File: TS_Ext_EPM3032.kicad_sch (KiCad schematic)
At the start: 52 parts, among them J1 JTAG, J2 CD_IN, J3 System Ext, J4 AUDIO OUT, J5 AudioJack3_SwitchTR, Q1 BC547, U1 EPM3064ALC44, U2 AMS1117, U3 YM2149, U4 YM2149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

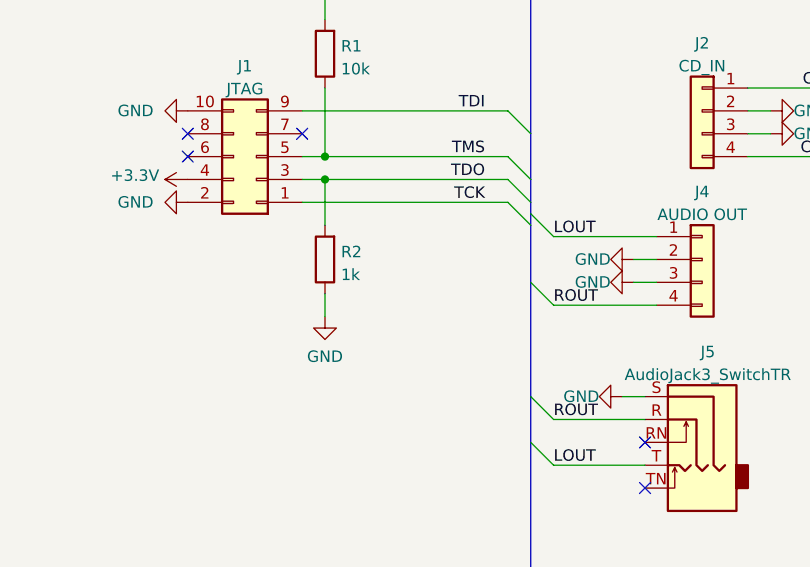
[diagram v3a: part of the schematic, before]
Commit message: Fix pull-up on JTAG connector
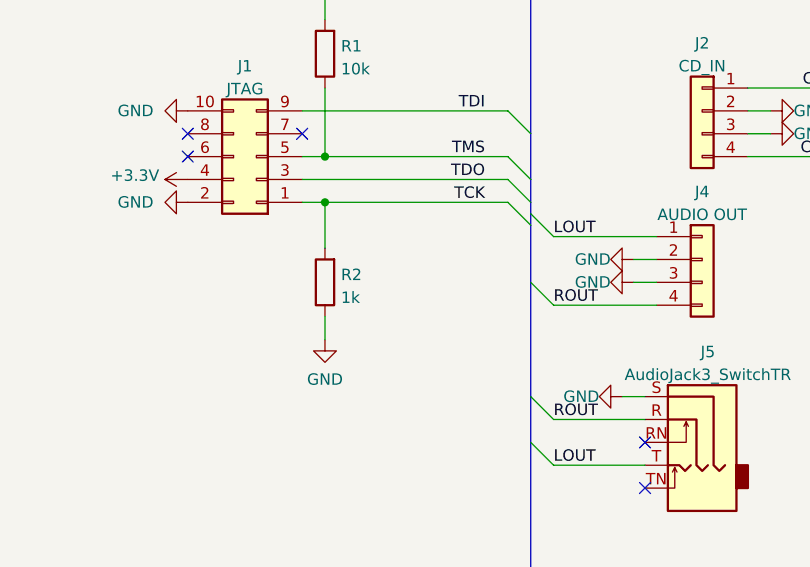
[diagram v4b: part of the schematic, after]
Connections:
- net TCK: now also R2.2
- net TDO: no longer R2.2
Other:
- moved on the sheet: R2
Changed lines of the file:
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@@
   (title_block
     (title "TurboSound Extension Card EPM3032")
-    (date "2022-11-06")
-    (rev "1.2")
+    (date "2023-01-24")
+    (rev "1.3")
     (company "ponchick")
     (comment 1 "Original schematic and firmware by MikhaelK")
@@
   (junction (at 297.18 102.87) (diameter 0) (color 0 0 0 0)
   )
+  (junction (at 78.74 144.78) (diameter 0) (color 0 0 0 0)
+  )
   (junction (at 139.7 266.7) (diameter 0) (color 0 0 0 0)
   )
@@
   (junction (at 129.54 45.72) (diameter 0) (color 0 0 0 0)
   )
-  (junction (at 78.74 142.24) (diameter 0) (color 0 0 0 0)
-  )
   (junction (at 271.78 60.96) (diameter 0) (color 0 0 0 0)
   )
@@
     (stroke (width 0) (type default) (color 0 0 0 0))
   )
-  (wire (pts (xy 78.74 157.48) (xy 78.74 154.94))
+  (wire (pts (xy 78.74 160.02) (xy 78.74 157.48))
     (stroke (width 0) (type default) (color 0 0 0 0))
   )
@@
     (stroke (width 0) (type default) (color 0 0 0 0))
   )
+  (wire (pts (xy 78.74 144.78) (xy 76.2 144.78))
+    (stroke (width 0) (type default) (color 0 0 0 0))
+  )
   (wire (pts (xy 142.24 147.32) (xy 152.4 147.32))
     (stroke (width 0) (type default) (color 0 0 0 0))
@@
     (stroke (width 0) (type default) (color 0 0 0 0))
   )
-  (wire (pts (xy 78.74 142.24) (xy 78.74 147.32))
+  (wire (pts (xy 78.74 144.78) (xy 78.74 149.86))
     (stroke (width 0) (type default) (color 0 0 0 0))
   )
@@
     (stroke (width 0) (type default) (color 0 0 0 0))
   )
-  (wire (pts (xy 99.06 144.78) (xy 76.2 144.78))
+  (wire (pts (xy 99.06 144.78) (xy 78.74 144.78))
     (stroke (width 0) (type default) (color 0 0 0 0))
   )
@@
     (stroke (width 0) (type default) (color 0 0 0 0))
   )
-  (wire (pts (xy 78.74 142.24) (xy 76.2 142.24))
-    (stroke (width 0) (type default) (color 0 0 0 0))
-  )
   (wire (pts (xy 142.24 139.7) (xy 152.4 139.7))
     (stroke (width 0) (type default) (color 0 0 0 0))
@@
     (stroke (width 0) (type default) (color 0 0 0 0))
   )
-  (wire (pts (xy 99.06 142.24) (xy 78.74 142.24))
+  (wire (pts (xy 76.2 142.24) (xy 99.06 142.24))
     (stroke (width 0) (type default) (color 0 0 0 0))
   )
@@
     (pin "2")
   )
-  (symbol (lib_id "power:GND") (at 78.74 157.48 0) (unit 1)
+  (symbol (lib_id "power:GND") (at 78.74 160.02 0) (unit 1)
     (in_bom yes) (on_board yes) (fields_autoplaced)
-    (property "Reference" "#PWR08" (id 0) (at 78.74 163.83 0)
+    (property "Reference" "#PWR08" (id 0) (at 78.74 166.37 0)
       (effects (font (size 1.27 1.27)) hide)
     )
-    (property "Value" "GND" (id 1) (at 78.74 161.9234 0))
-    (property "Footprint" "" (id 2) (at 78.74 157.48 0)
+    (property "Value" "GND" (id 1) (at 78.74 164.4634 0))
+    (property "Footprint" "" (id 2) (at 78.74 160.02 0)
       (effects (font (size 1.27 1.27)) hide)
     )
-    (property "Datasheet" "" (id 3) (at 78.74 157.48 0)
+    (property "Datasheet" "" (id 3) (at 78.74 160.02 0)
       (effects (font (size 1.27 1.27)) hide)
     )
@@
     (pin "8")
   )
-  (symbol (lib_id "Device:R") (at 78.74 151.13 180) (unit 1)
+  (symbol (lib_id "Device:R") (at 78.74 153.67 180) (unit 1)
     (in_bom yes) (on_board yes) (fields_autoplaced)
-    (property "Reference" "R2" (id 0) (at 80.518 150.2953 0)
+    (property "Reference" "R2" (id 0) (at 80.518 152.8353 0)
       (effects (font (size 1.27 1.27)) (justify right))
     )
-    (property "Value" "1k" (id 1) (at 80.518 152.8322 0)
+    (property "Value" "1k" (id 1) (at 80.518 155.3722 0)
       (effects (font (size 1.27 1.27)) (justify right))
     )
-    (property "Footprint" "Resistor_THT:R_Axial_DIN0204_L3.6mm_D1.6mm_P7.62mm_Horizontal" (id 2) (at 80.518 151.13 90)
+    (property "Footprint" "Resistor_THT:R_Axial_DIN0204_L3.6mm_D1.6mm_P7.62mm_Horizontal" (id 2) (at 80.518 153.67 90)
       (effects (font (size 1.27 1.27)) hide)
     )
-    (property "Datasheet" "~" (id 3) (at 78.74 151.13 0)
+    (property "Datasheet" "~" (id 3) (at 78.74 153.67 0)
       (effects (font (size 1.27 1.27)) hide)
     )

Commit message: Migrated to KiCad 8, CPLD value fix
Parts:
- J3: now left out of the parts list
- J5: value AudioJack3_SwitchTR -> SJ1-3525N; symbol Connector:AudioJack3_SwitchTR -> Connector_Audio:AudioJack3_SwitchTR
- U1: value EPM3064ALC44 -> EPM3032ALC44
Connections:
- net ~{RDR}: no longer names the net of J3.b15 (Pin_b15)
- no-connect marks 83 -> 84
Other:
- moved on the sheet: J4, J5

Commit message: Change C13/C14 to electrolytic
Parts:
- C13, C14: footprint Capacitor_THT:C_Rect_L7.0mm_W2.0mm_P5.00mm -> Capacitor_THT:CP_Radial_D5.0mm_P2.50mm; symbol Device:C -> Device:C_Polarized
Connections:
- net ROUT: now also C14.2; no longer C14.1
- net at R24.2, U5.7: now also C14.1; no longer C14.2
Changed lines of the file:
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@@
 		(title "TurboSound Extension Card EPM3032")
 		(date "2024-04-10")
-		(rev "1.4")
+		(rev "1.5")
 		(company "ponchick")
 		(comment 1 "Original schematic and firmware by MikhaelK")
@@
 	)
 	(symbol
-		(lib_id "Device:C")
-		(at 325.12 100.33 270)
+		(lib_id "Device:C_Polarized")
+		(at 325.12 100.33 90)
 		(unit 1)
 		(exclude_from_sim no)
@@
 		(fields_autoplaced yes)
 		(property "Reference" "C14"
-			(at 325.12 94.4712 90)
+			(at 324.231 92.71 90)
 			(effects
 				(font
@@
 		)
 		(property "Value" "10u"
-			(at 325.12 97.0081 90)
+			(at 324.231 95.25 90)
 			(effects
 				(font
@@
 			)
 		)
-		(property "Footprint" "Capacitor_THT:C_Rect_L7.0mm_W2.0mm_P5.00mm"
-			(at 321.31 101.2952 0)
+		(property "Footprint" "Capacitor_THT:CP_Radial_D5.0mm_P2.50mm"
+			(at 328.93 99.3648 0)
 			(effects
 				(font
@@
 			)
 		)
-		(property "Datasheet" ""
+		(property "Datasheet" "~"
 			(at 325.12 100.33 0)
 			(effects
@@
 			)
 		)
-		(property "Description" ""
+		(property "Description" "Polarized capacitor"
 			(at 325.12 100.33 0)
 			(effects
@@
 	)
 	(symbol
-		(lib_id "Device:C")
+		(lib_id "Device:C_Polarized")
 		(at 325.12 53.34 90)
 		(unit 1)
@@
 		(fields_autoplaced yes)
 		(property "Reference" "C13"
-			(at 325.12 47.4812 90)
+			(at 324.231 45.72 90)
 			(effects
 				(font
@@
 		)
 		(property "Value" "10u"
-			(at 325.12 50.0181 90)
+			(at 324.231 48.26 90)
 			(effects
 				(font
@@
 			)
 		)
-		(property "Footprint" "Capacitor_THT:C_Rect_L7.0mm_W2.0mm_P5.00mm"
+		(property "Footprint" "Capacitor_THT:CP_Radial_D5.0mm_P2.50mm"
 			(at 328.93 52.3748 0)
 			(effects
@@
 			)
 		)
-		(property "Datasheet" ""
+		(property "Datasheet" "~"
 			(at 325.12 53.34 0)
 			(effects
@@
 			)
 		)
-		(property "Description" ""
+		(property "Description" "Polarized capacitor"
 			(at 325.12 53.34 0)
 			(effects
